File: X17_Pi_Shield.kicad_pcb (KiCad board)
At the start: 2 copper layers, 4 parts, among them J1 BM04B-GHS-TBT, U1 RASPBERRY_PI_4B_4GB, U2 BNO080

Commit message: Adding Libraries
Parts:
- removed Bar02: DF13-4P-1.25DSA, Connector_Hirose:Hirose_DF13-04P-1.25DS_1x04_P1.25mm_Horizontal
- added D3: MBR0520LT, Diode_SMD:D_SOD-123, F.Cu at (187.3, 82.2)
- added D9: MBR0520LT, Diode_SMD:D_SOD-123, F.Cu at (187.3, 85.5)
- added J19: 430450212, 0430450212/:CON_430450212_MOL, F.Cu at (185.9, 101.0)
- added J2: BM02B-GHS-TBT, leak_footprint:CONN_BM02B-GHS-TBT_JST, F.Cu at (173.4, 54.8)
- added J3: BM02B-GHS-TBT, leak_footprint:CONN_BM02B-GHS-TBT_JST, F.Cu at (173.4, 61.6)
- added J4: BM02B-GHS-TBT, leak_footprint:CONN_BM02B-GHS-TBT_JST, F.Cu at (173.4, 68.4)
- added J5: BM02B-GHS-TBT, leak_footprint:CONN_BM02B-GHS-TBT_JST, F.Cu at (173.4, 75.2)
- added J6: Conn_01x03_Pin, Connector_PinHeader_2.54mm:PinHeader_1x03_P2.54mm_Vertical, F.Cu at (182.0, 61.2)
- added J9: 430450612, CON_430450612_MOL:CON_430450612_MOL, F.Cu at (178.4, 88.6)
- added U10: 4754, 4754:MODULE_4754, F.Cu at (88.4, 148.1)
- added U3: INA260AIPW, INA260AIPW:SOP65P640X120-16N, F.Cu at (171.9, 110.6)
- added U8: RASPBERRY_PI_4B_4GB, RASPBERRY_PI_4B_4GB:MODULE_RASPBERRY_PI_4B_4GB, F.Cu at (119.2, 80.0)
- added U9: ISO3086TDW, ISO3086TDW:SOIC127P1030X265-16N, F.Cu at (174.0, 98.8)
- U1: value RASPBERRY_PI_4B_4GB -> 4754; footprint RASPBERRY_PI_4B_4GB:MODULE_RASPBERRY_PI_4B_4GB -> 4754:MODULE_4754
- U2: value BNO080 -> TPS2117DRLR; footprint BNO080:IC_BNO080 -> TPS2117DRLR:SOTFL50P160X60-8N
- moved J1 115.6 mm to (185.0, 55.0)
- moved U2 88.3 mm to (169.3, 115.7)
- moved U1 81.4 mm to (88.4, 123.0)
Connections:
- J1 pad 1: unconnected-(J1-Pad1) -> +5V
- J1 pad 2: unconnected-(J1-Pad2) -> /Pi + IMU/SCL
- J1 pad 3: unconnected-(J1-Pad3) -> /Pi + IMU/SDA
- J1 pad 4: unconnected-(J1-Pad4) -> GND
- U2 pad 1: (no net) -> GND
- U2 pad 2: GND -> /Power/5V_TOTAL
- U2 pad 3: +3V3 -> /Power/5V_BACKPLANE
- U2 pad 4: unconnected-(U2-~{BOOT}-Pad4) -> Net-(U2-PR1)
- U2 pad 5: unconnected-(U2-PS1-Pad5) -> /Power/5V_BACKPLANE
- U2 pad 6: unconnected-(U2-PS0/WAKE-Pad6) -> /Power/5V_WALL_IN
- U2 pad 7: (no net) -> /Power/5V_TOTAL
- U2 pad 8: (no net) -> Net-(U2-ST)

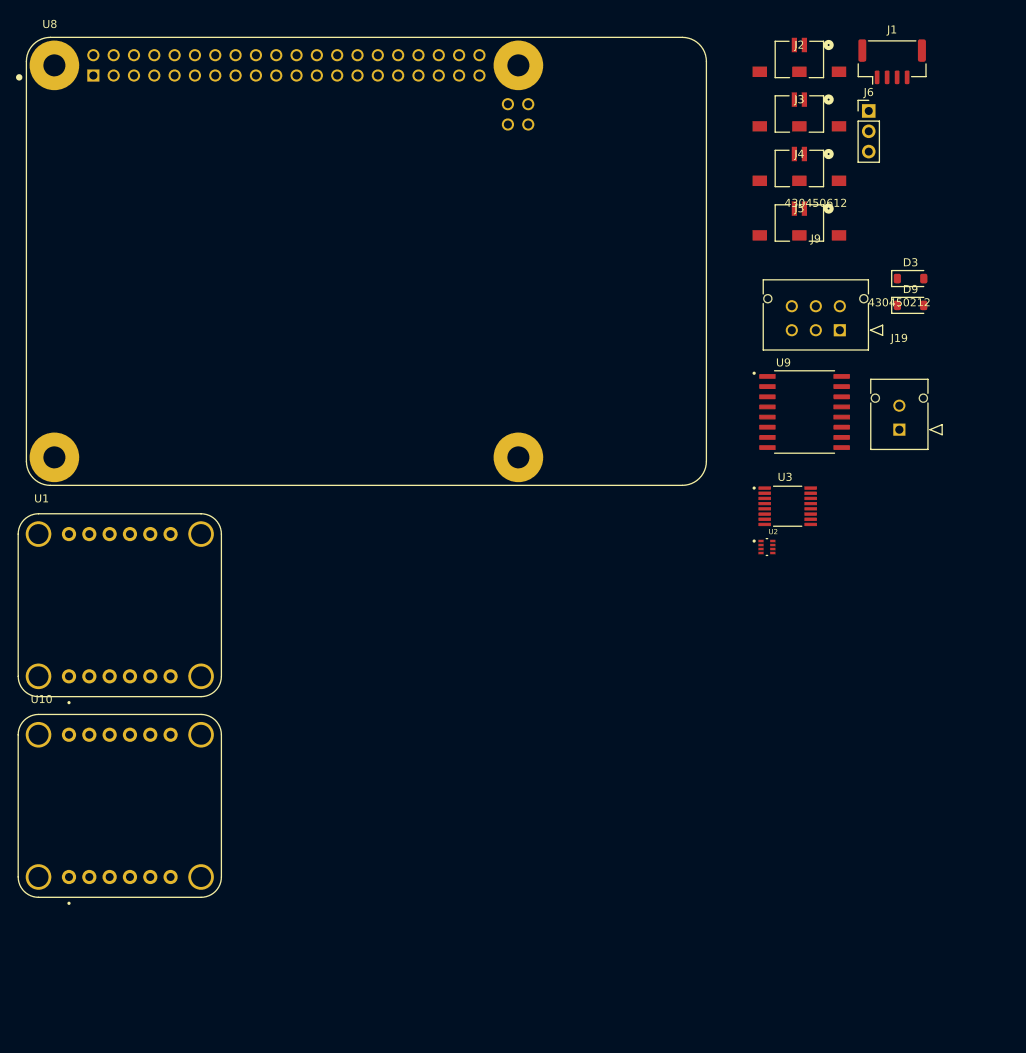
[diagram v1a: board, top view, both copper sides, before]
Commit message: board dimensions
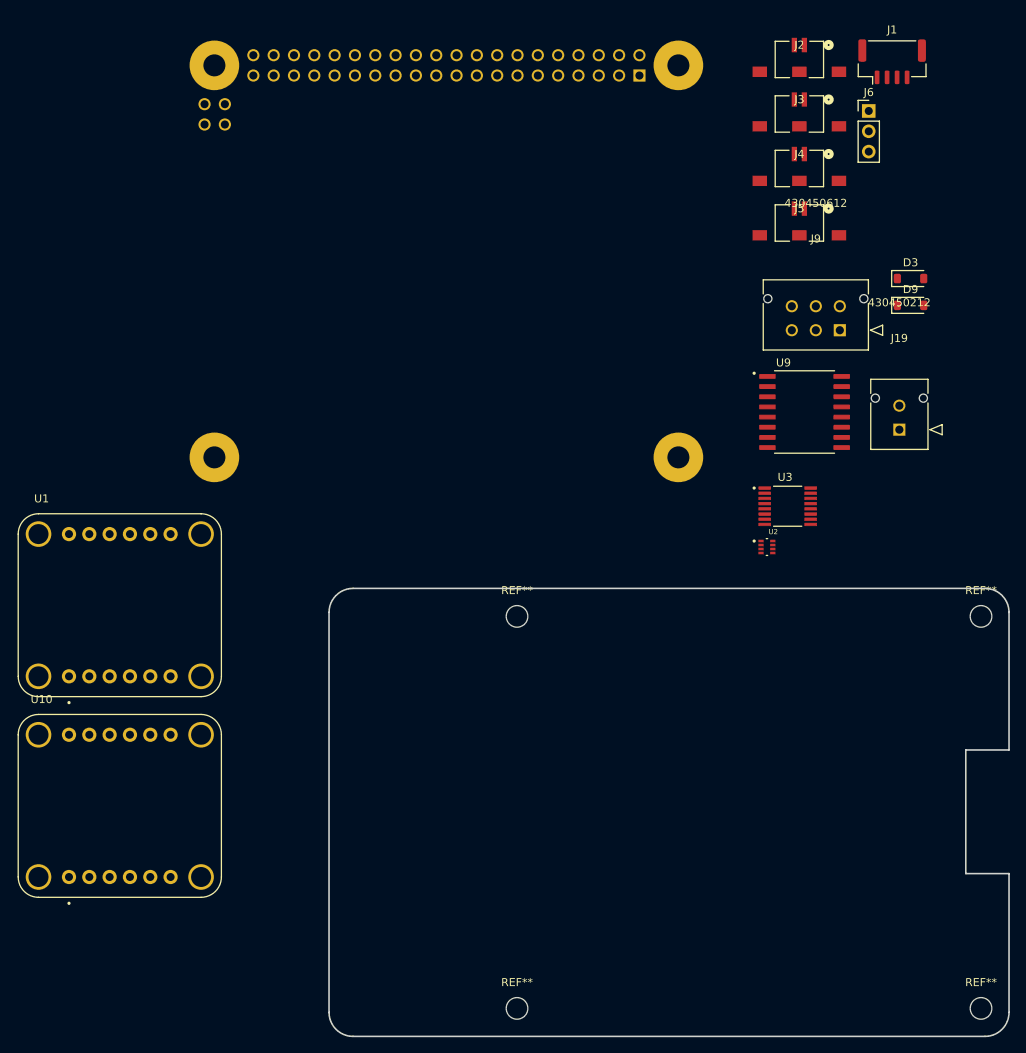
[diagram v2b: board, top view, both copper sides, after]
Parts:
- added REF**: MountingHole_2.7mm_M2.5_ISO14580, MountingHole:MountingHole_2.7mm_M2.5_ISO14580, F.Cu at (138.1, 124.4)
- added REF**: MountingHole_2.7mm_M2.5_ISO14580, MountingHole:MountingHole_2.7mm_M2.5_ISO14580, F.Cu at (196.1, 173.4)
- added REF**: MountingHole_2.7mm_M2.5_ISO14580, MountingHole:MountingHole_2.7mm_M2.5_ISO14580, F.Cu at (196.1, 124.4)
- added REF**: MountingHole_2.7mm_M2.5_ISO14580, MountingHole:MountingHole_2.7mm_M2.5_ISO14580, F.Cu at (138.1, 173.4)
- U8: moved to B.Cu
- turned U8 to 180 degrees
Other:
- board outline added: 85 x 56 mm

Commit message: Pre-Toolbox Final
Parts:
- removed D3, D9: MBR0520LT, Diode_SMD:D_SOD-123
- removed REF** (x4): MountingHole_2.7mm_M2.5_ISO14580, MountingHole:MountingHole_2.7mm_M2.5_ISO14580
- added C1: 10uF, Capacitor_SMD:C_0805_2012Metric_Pad1.18x1.45mm_HandSolder, F.Cu at (157.9, 49.7)
- added C10: 0.1uF, Capacitor_SMD:C_0805_2012Metric_Pad1.18x1.45mm_HandSolder, F.Cu at (157.9, 67.7)
- added C11: 10nF, Capacitor_SMD:C_0805_2012Metric_Pad1.18x1.45mm_HandSolder, F.Cu at (157.9, 70.7)
- added C12: 10uF, Capacitor_SMD:C_0805_2012Metric_Pad1.18x1.45mm_HandSolder, F.Cu at (92.8, 139.3)
- added C13: 10uF, Capacitor_SMD:C_0805_2012Metric_Pad1.18x1.45mm_HandSolder, F.Cu at (92.8, 142.3)
- added C14: 0.1uF, Capacitor_SMD:C_0805_2012Metric_Pad1.18x1.45mm_HandSolder, F.Cu at (157.9, 73.8)
- added C15: 10uF, Capacitor_SMD:C_0805_2012Metric_Pad1.18x1.45mm_HandSolder, F.Cu at (92.8, 145.3)
- added C16: 10uF, Capacitor_SMD:C_0805_2012Metric_Pad1.18x1.45mm_HandSolder, F.Cu at (92.8, 148.3)
- added C17: 150uF, Capacitor_SMD:C_0805_2012Metric_Pad1.18x1.45mm_HandSolder, F.Cu at (167.4, 87.8)
- added C18: 10uF, Capacitor_SMD:C_0805_2012Metric_Pad1.18x1.45mm_HandSolder, F.Cu at (167.4, 90.8)
- added C19: 0.1uF, Capacitor_SMD:C_0805_2012Metric_Pad1.18x1.45mm_HandSolder, F.Cu at (167.4, 93.8)
- added C2: 4.7uF, Capacitor_SMD:C_0805_2012Metric_Pad1.18x1.45mm_HandSolder, F.Cu at (157.9, 52.7)
- added C20: 0.1uF, Capacitor_SMD:C_0805_2012Metric_Pad1.18x1.45mm_HandSolder, F.Cu at (167.4, 96.8)
- added C21: 22uF, Capacitor_SMD:C_0805_2012Metric_Pad1.18x1.45mm_HandSolder, F.Cu at (167.4, 99.8)
- added C3: 10uF, Capacitor_SMD:C_0805_2012Metric_Pad1.18x1.45mm_HandSolder, F.Cu at (157.9, 55.7)
- added C5: 150uF, Capacitor_SMD:C_0805_2012Metric_Pad1.18x1.45mm_HandSolder, F.Cu at (167.4, 84.8)
- added C7: 10uF, Capacitor_SMD:C_0805_2012Metric_Pad1.18x1.45mm_HandSolder, F.Cu at (157.9, 58.7)
- added C8: 0.1uF, Capacitor_SMD:C_0805_2012Metric_Pad1.18x1.45mm_HandSolder, F.Cu at (157.9, 61.7)
- added C9: 4.7uF, Capacitor_SMD:C_0805_2012Metric_Pad1.18x1.45mm_HandSolder, F.Cu at (157.9, 64.7)
- added D2: LED, LED_SMD:LED_0805_2012Metric_Pad1.15x1.40mm_HandSolder, F.Cu at (162.6, 84.8)
- added D4: LED, LED_SMD:LED_0805_2012Metric_Pad1.15x1.40mm_HandSolder, F.Cu at (162.6, 87.8)
- added D5: LED, LED_SMD:LED_0805_2012Metric_Pad1.15x1.40mm_HandSolder, F.Cu at (162.6, 90.8)
- added D6: LED, LED_SMD:LED_0805_2012Metric_Pad1.15x1.40mm_HandSolder, F.Cu at (162.6, 93.9)
- added D7: LED, LED_SMD:LED_0805_2012Metric_Pad1.15x1.40mm_HandSolder, F.Cu at (162.6, 96.9)
- added D8: LED, LED_SMD:LED_0805_2012Metric_Pad1.15x1.40mm_HandSolder, F.Cu at (162.6, 100.0)
- added J10: BM04B-GHS-TBT, Connector_JST:JST_GH_BM04B-GHS-TBT_1x04-1MP_P1.25mm_Vertical, F.Cu at (95.6, 111.5)
- added J11: BM04B-GHS-TBT, Connector_JST:JST_GH_BM04B-GHS-TBT_1x04-1MP_P1.25mm_Vertical, F.Cu at (95.6, 119.2)
- added J12: Conn_01x05_Pin, Connector_PinHeader_2.54mm:PinHeader_1x05_P2.54mm_Vertical, F.Cu at (92.7, 125.3)
- added J13: Conn_01x03_Pin, Connector_PinHeader_2.54mm:PinHeader_1x05_P2.54mm_Vertical, F.Cu at (97.3, 125.3)
- added J14: Conn_01x03_Pin, Connector_PinHeader_2.54mm:PinHeader_1x03_P2.54mm_Vertical, F.Cu at (97.5, 140.1)
- added J20: Conn_01x02_Pin, Connector_PinHeader_2.54mm:PinHeader_1x02_P2.54mm_Vertical, F.Cu at (176.5, 101.5)
- added J21: Conn_01x02_Pin, Connector_PinHeader_2.54mm:PinHeader_1x02_P2.54mm_Vertical, F.Cu at (181.2, 101.5)
- added J7: BM04B-GHS-TBT, Connector_JST:JST_GH_BM04B-GHS-TBT_1x04-1MP_P1.25mm_Vertical, F.Cu at (173.4, 123.3)
- added J8: UJC-HP-L-G-5-MSMT-TR, UJC_HP_L_G_5_MSMT_TR:CUI_UJC-HP-L-G-5-MSMT-TR, F.Cu at (176.7, 89.1)
- added JP1: SolderJumper_2_Open, Jumper:SolderJumper-2_P1.3mm_Open_RoundedPad1.0x1.5mm, F.Cu at (172.0, 94.4)
- added JP2: SolderJumper_2_Open, Jumper:SolderJumper-2_P1.3mm_Open_RoundedPad1.0x1.5mm, F.Cu at (172.0, 98.0)
- added JP3: SolderJumper_2_Open, Jumper:SolderJumper-2_P1.3mm_Open_RoundedPad1.0x1.5mm, F.Cu at (172.0, 101.5)
- added JP4: SolderJumper_2_Open, Jumper:SolderJumper-2_P1.3mm_Open_RoundedPad1.0x1.5mm, F.Cu at (172.0, 105.1)
- added R1: 1K, Resistor_SMD:R_0805_2012Metric_Pad1.20x1.40mm_HandSolder, F.Cu at (170.6, 128.6)
- added R10: 10k, Resistor_SMD:R_0805_2012Metric_Pad1.20x1.40mm_HandSolder, F.Cu at (162.7, 73.9)
- added R11: 10k, Resistor_SMD:R_0805_2012Metric_Pad1.20x1.40mm_HandSolder, F.Cu at (181.8, 77.2)
- added R12: 240, Resistor_SMD:R_0805_2012Metric_Pad1.20x1.40mm_HandSolder, F.Cu at (157.8, 87.7)
- added R13: 240, Resistor_SMD:R_0805_2012Metric_Pad1.20x1.40mm_HandSolder, F.Cu at (157.8, 90.6)
- added R14: 240, Resistor_SMD:R_0805_2012Metric_Pad1.20x1.40mm_HandSolder, F.Cu at (157.8, 93.6)
- added R15: 240, Resistor_SMD:R_0805_2012Metric_Pad1.20x1.40mm_HandSolder, F.Cu at (157.8, 96.5)
- added R16: 240, Resistor_SMD:R_0805_2012Metric_Pad1.20x1.40mm_HandSolder, F.Cu at (157.8, 99.5)
- added R17: 20k, Resistor_SMD:R_0805_2012Metric_Pad1.20x1.40mm_HandSolder, F.Cu at (162.7, 79.8)
- added R18: 1K, Resistor_SMD:R_0805_2012Metric_Pad1.20x1.40mm_HandSolder, F.Cu at (157.8, 102.4)
- added R2: 27K, Resistor_SMD:R_0805_2012Metric_Pad1.20x1.40mm_HandSolder, F.Cu at (170.6, 131.5)
- added R21: 1K, Resistor_SMD:R_0805_2012Metric_Pad1.20x1.40mm_HandSolder, F.Cu at (157.8, 105.4)
- added R22: 2K, Resistor_SMD:R_0805_2012Metric_Pad1.20x1.40mm_HandSolder, F.Cu at (157.8, 108.3)
- added R3: 1K, Resistor_SMD:R_0805_2012Metric_Pad1.20x1.40mm_HandSolder, F.Cu at (170.6, 134.5)
- added R4: 240, Resistor_SMD:R_0805_2012Metric_Pad1.20x1.40mm_HandSolder, F.Cu at (170.6, 137.4)
- added R5: 10k, Resistor_SMD:R_0805_2012Metric_Pad1.20x1.40mm_HandSolder, F.Cu at (162.7, 62.1)
- added R6: 240, Resistor_SMD:R_0805_2012Metric_Pad1.20x1.40mm_HandSolder, F.Cu at (157.8, 84.7)
- added R7: 10k, Resistor_SMD:R_0805_2012Metric_Pad1.20x1.40mm_HandSolder, F.Cu at (162.7, 65.0)
- added R8: 10k, Resistor_SMD:R_0805_2012Metric_Pad1.20x1.40mm_HandSolder, F.Cu at (162.7, 68.0)
- added R9: 20k, Resistor_SMD:R_0805_2012Metric_Pad1.20x1.40mm_HandSolder, F.Cu at (162.7, 70.9)
- added U5: MAX485, MAX485:SO08, F.Cu at (181.4, 64.8)
- U8: moved to F.Cu
- moved J6 68.6 mm to (175.2, 129.4)
- moved J1 61.7 mm to (173.4, 115.6)
- moved J2 61.7 mm to (161.8, 115.3)
- moved J4 61.7 mm to (161.8, 129.0)
- moved J5 61.7 mm to (161.8, 135.8)
- moved J3 61.7 mm to (161.8, 122.1)
- moved J19 44.8 mm to (183.0, 56.3)
- moved J9 33.0 mm to (171.7, 56.3)
- moved U9 32.4 mm to (172.0, 66.5)
- moved U3 16.3 mm to (179.1, 95.9)
- moved U2 12.7 mm to (167.3, 103.1)
- moved U1 11.9 mm to (76.9, 119.9)
- moved U10 11.9 mm to (76.9, 145.0)
- moved U8 11.9 mm to (107.7, 76.9), turned to 0 degrees
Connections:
- J1 pad 1: +5V -> +3V3
- U1 pad JP1_2: +3V3 -> unconnected-(U1-3VO-PadJP1_2)
- U10 pad JP1_2: +3V3 -> unconnected-(U10-3VO-PadJP1_2)
- U2 pad 7: /Power/5V_TOTAL -> unconnected-(U2-VOUT__1-Pad7)
- U8 pad 16: unconnected-(U8-GPIO23/GPIO_GEN4-Pad16) -> /Pi + IMU/LEAK
- U8 pad 26: /Pi + IMU/CE1 -> unconnected-(U8-GPIO7/~{SPI_CE1}-Pad26)
- U8 pad 32: /Pi + IMU/BKP_EN -> /Pi + IMU/TX_TB
- U8 pad 33: /Pi + IMU/TB_EN -> /Pi + IMU/RX_TB
- U8 pad 35: /Pi + IMU/LEAK -> /Pi + IMU/BKP_EN
- U8 pad 38: unconnected-(U8-GPIO20-Pad38) -> /Pi + IMU/TB_EN
- U8 pad S1: Net-(U8-SHIELD-PadS1) -> unconnected-(U8-SHIELD-PadS1)
- U8 pad S2: Net-(U8-SHIELD-PadS1) -> unconnected-(U8-SHIELD-PadS1)_2
- U8 pad S3: Net-(U8-SHIELD-PadS1) -> unconnected-(U8-SHIELD-PadS1)_1
- U8 pad S4: Net-(U8-SHIELD-PadS1) -> unconnected-(U8-SHIELD-PadS1)_3
- U9 pad 16: GND_TB -> Net-(U6-VOUT)
- U9 pad 5: /Pi + IMU/RX -> /Pi + IMU/RX_TB
- U9 pad 8: /Pi + IMU/TX -> /Pi + IMU/TX_TB
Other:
- board size 85 x 56 mm -> 9.3 x 6.9 mm

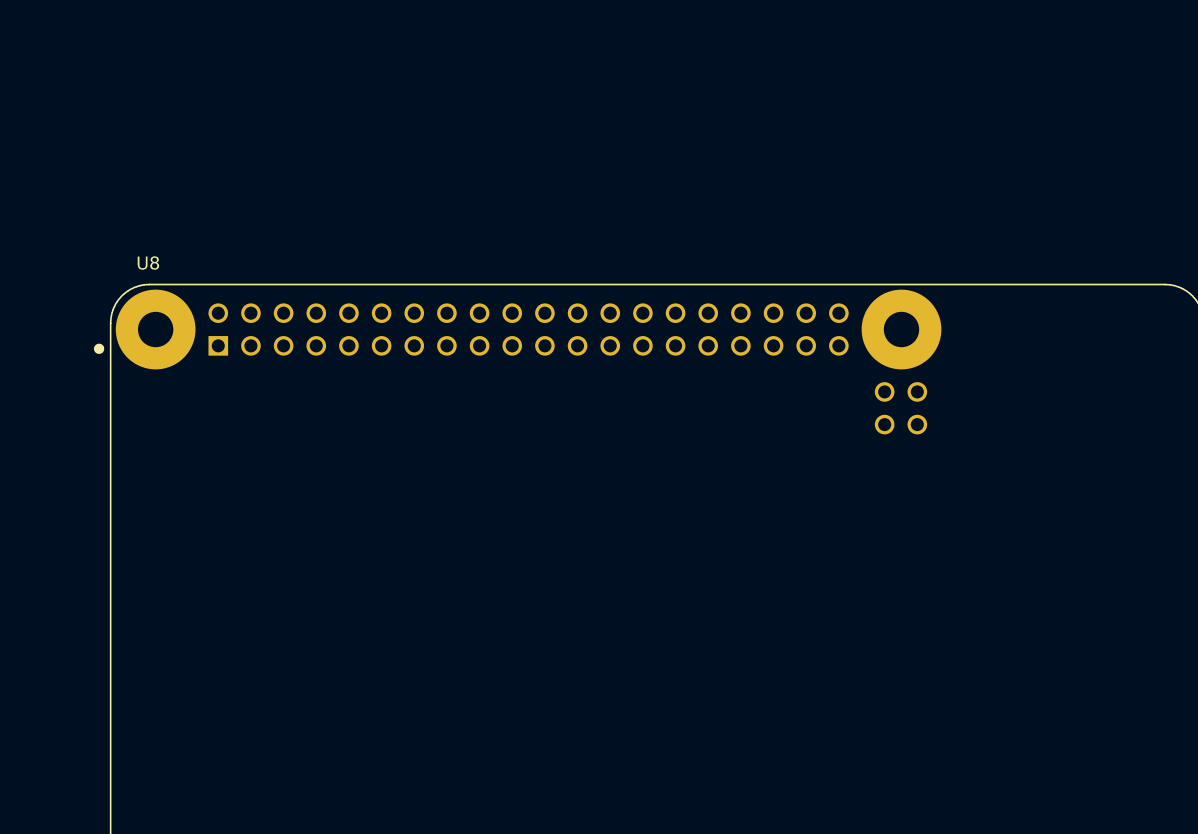
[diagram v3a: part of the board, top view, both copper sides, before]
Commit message: re-add dimensions
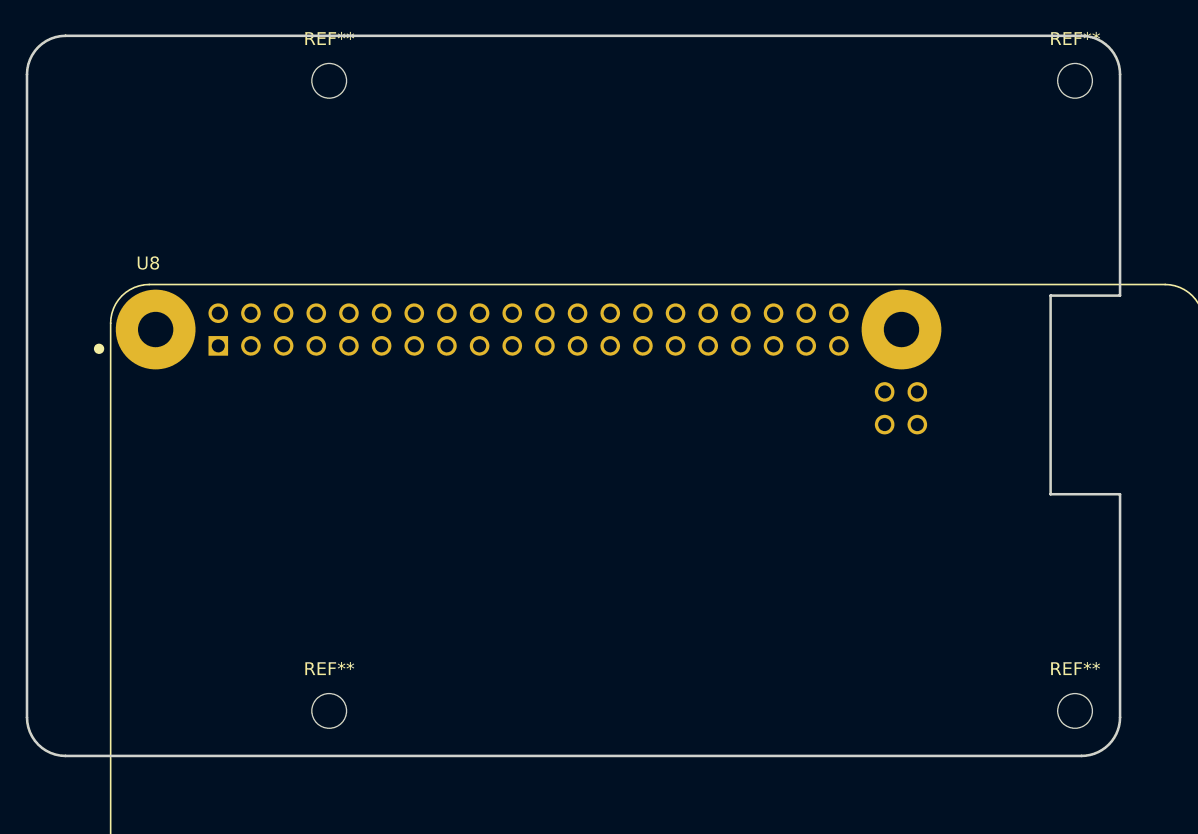
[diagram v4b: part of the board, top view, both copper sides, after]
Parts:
- added REF**: MountingHole_2.7mm_M2.5_ISO14580, MountingHole:MountingHole_2.7mm_M2.5_ISO14580, F.Cu at (82.2, 82.1)
- added REF**: MountingHole_2.7mm_M2.5_ISO14580, MountingHole:MountingHole_2.7mm_M2.5_ISO14580, F.Cu at (140.2, 82.1)
- added REF**: MountingHole_2.7mm_M2.5_ISO14580, MountingHole:MountingHole_2.7mm_M2.5_ISO14580, F.Cu at (140.2, 33.1)
- added REF**: MountingHole_2.7mm_M2.5_ISO14580, MountingHole:MountingHole_2.7mm_M2.5_ISO14580, F.Cu at (82.2, 33.1)
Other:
- board size 9.3 x 6.9 mm -> 85 x 56 mm

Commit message: Finalized Footprints
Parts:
- added C1: 10uF, Capacitor_SMD:C_0603_1608Metric_Pad1.08x0.95mm_HandSolder, F.Cu at (-5.63, -17.6)
- added C10: 0.1uF, Capacitor_SMD:C_0603_1608Metric_Pad1.08x0.95mm_HandSolder, F.Cu at (-1.28, -10.1)
- added C2: 1uF, Capacitor_SMD:C_0603_1608Metric_Pad1.08x0.95mm_HandSolder, F.Cu at (-5.63, -15.1)
- added C3: 10nF, Capacitor_SMD:C_0603_1608Metric_Pad1.08x0.95mm_HandSolder, F.Cu at (-5.63, -12.6)
- added C4: 10uF, Capacitor_SMD:C_0603_1608Metric_Pad1.08x0.95mm_HandSolder, F.Cu at (-5.63, -10.1)
- added C6: 1uF, Capacitor_SMD:C_0603_1608Metric_Pad1.08x0.95mm_HandSolder, F.Cu at (-5.63, -7.56)
- added C7: 10nF, Capacitor_SMD:C_0603_1608Metric_Pad1.08x0.95mm_HandSolder, F.Cu at (-1.28, -17.6)
- added C8: 0.1uF, Capacitor_SMD:C_0603_1608Metric_Pad1.08x0.95mm_HandSolder, F.Cu at (-1.28, -15.1)
- added C9: 10uF, Capacitor_SMD:C_0603_1608Metric_Pad1.08x0.95mm_HandSolder, F.Cu at (-1.28, -12.6)
- added D1: LED, LED_SMD:LED_0805_2012Metric_Pad1.15x1.40mm_HandSolder, F.Cu at (3.86, 0.46)
- added FB1: FerriteBead, BLM18KN331EH1D:BLM18_MUR-M, F.Cu at (8.17, -17.3)
- added FB2: FerriteBead, BLM18KN331EH1D:BLM18_MUR-M, F.Cu at (8.17, -14.1)
- added FB3: FerriteBead, BLM18KN331EH1D:BLM18_MUR-M, F.Cu at (8.17, -11.0)
- added FB4: FerriteBead, BLM18KN331EH1D:BLM18_MUR-M, F.Cu at (8.17, -7.80)
- added FB5: FerriteBead, BLM18KN331EH1D:BLM18_MUR-M, F.Cu at (8.17, -4.64)
- added J22: 430450212, 0430450212/:CON_430450212_MOL, F.Cu at (-16.1, -23.1)
- added J23: 430450612, CON_430450612_MOL:CON_430450612_MOL, F.Cu at (12.5, -23.1)
- added J24: 430450212, 0430450212/:CON_430450212_MOL, F.Cu at (-4.81, -23.1)
- added J9: Conn_01x04_Pin, Connector_PinHeader_2.54mm:PinHeader_1x04_P2.54mm_Vertical, F.Cu at (-2.88, 1.26)
- added R17: 120, Resistor_SMD:R_0603_1608Metric_Pad0.98x0.95mm_HandSolder, F.Cu at (3.07, -15.1)
- added R19: 10k, Resistor_SMD:R_0603_1608Metric_Pad0.98x0.95mm_HandSolder, F.Cu at (3.07, -12.6)
- added R20: 10k, Resistor_SMD:R_0603_1608Metric_Pad0.98x0.95mm_HandSolder, F.Cu at (3.07, -10.1)
- added R5: 120, Resistor_SMD:R_0603_1608Metric_Pad0.98x0.95mm_HandSolder, F.Cu at (-1.28, -7.56)
- added R9: 5k, Resistor_SMD:R_0603_1608Metric_Pad0.98x0.95mm_HandSolder, F.Cu at (3.07, -17.6)
- added TP1: TestPoint, TestPoint:TestPoint_Pad_D3.0mm, F.Cu at (-19.0, 1.46)
- added TP2: TestPoint, TestPoint:TestPoint_Pad_D3.0mm, F.Cu at (-19.0, 6.51)
- added TP3: TestPoint, TestPoint:TestPoint_Pad_D3.0mm, F.Cu at (-19.0, 11.6)
- added U4: AZ1117IH-3.3TRG1, AZ1117IH_3_3TRG1:SOT223_AZ1117I_6P5X3P5_DIO-M, F.Cu at (-11.3, 4.20)
- added U6: MMBT3906LT3G, MMBT3906LT3G:SOT-23-3_1P4X3P040_ONS, F.Cu at (3.80, 4.48)
- added U7: ISOW1432BDFMR, ISOW1432BDFMR:SOIC127P1030X355-20N, F.Cu at (-14.3, -11.7)
- C12, C13, C14, C15, C16, C17, C18, C19, C20, C21, C5: footprint Capacitor_SMD:C_0805_2012Metric_Pad1.18x1.45mm_HandSolder -> Capacitor_SMD:C_0603_1608Metric_Pad1.08x0.95mm_HandSolder
- R1, R10, R11, R12, R13, R14, R15, R16, R18, R2, R21, R22, R3, R4, R6: footprint Resistor_SMD:R_0805_2012Metric_Pad1.20x1.40mm_HandSolder -> Resistor_SMD:R_0603_1608Metric_Pad0.98x0.95mm_HandSolder
- U5: footprint MAX485:SO08 -> AZ1117IH_3_3TRG1:SOT223_AZ1117I_6P5X3P5_DIO-M
- moved U8 91.4 mm to (34.0, 131.0)
- moved REF** 45.0 mm to (38.8, 70.2)
- moved REF** 45.0 mm to (38.8, 21.2)
- moved REF** 45.0 mm to (96.8, 70.2)
- moved REF** 45.0 mm to (96.8, 21.2)
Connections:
- C14 pad 2: /Power/5V_BACKPLANE -> Net-(U5-A)
- R10 pad 1: /Power/5V_BACKPLANE -> +5V
- R11 pad 1: GND -> Net-(U5-B)
- R11 pad 2: Net-(U5-B) -> GND
- U8 pad 18: unconnected-(U8-GPIO24/GPIO_GEN5-Pad18) -> /Pi + IMU/ISO_FLT
- U8 pad 40: unconnected-(U8-GPIO21-Pad40) -> /Pi + IMU/NRST_TB
